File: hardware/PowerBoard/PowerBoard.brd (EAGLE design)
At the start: 90 x 56 mm, 136 parts, among them J1 CON-HRS-DM3AT, J2 CON-ZX62R-B-5P, J3 CON-FTSH-105-01-L-DV-K, J4 CON-S2B-PH-SM4-TB, J5 CON-PJ-102A, J6 CON-71741-0002-TOP, J7 SWITCH-CJS-1200-1200, M1 MOUNT-HOLE3.3, M2 MOUNT-HOLE3.3, M3 MOUNT-HOLE3.3, M4 MOUNT-HOLE3.3, M5 FIDUCIAL1X2, M6 FIDUCIAL1X2, M7 FIDUCIAL1X2, M8 FIDUCIAL1X2, Q1 SI2323CDS, Q2 SI2312CDS, Q3 SI2333CDS, Q4 SI2333CDS, SW1 SWITCH-SPST, SW2 SWITCH-MS12ASG30, SW3 SWITCH-ESWITCH-TL3340G, U1 LTC4361-2DC, U10 MAX9938FEUK, U11 MAX9938FEUK, U12 MAX9938FEUK, U13 STM32F10XCXT6, U14 LTC2942-1, U15 USBLC6-2, U2 LTC4085, U3 XC6220B331MR-G, U4 XC6220B331MR-G, U5 XC9236A15DMR-G, U6 MIC94043, U8 MAX9938FEUK, U9 MAX9938FEUK, X1 ECX-2236, X2 ECX-31B

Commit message: - Layout update
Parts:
- moved R12 0.50 mm to (36.0, 36.5)
- moved R14 0.50 mm to (41.6, 36.5)
- moved R41 0.50 mm to (38.8, 37.3)
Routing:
- net D1V5-EN: track 10.7 -> 11.2 mm
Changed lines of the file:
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@@
 <layer number="21" name="tPlace" color="7" fill="1" visible="no" active="yes"/>
 <layer number="22" name="bPlace" color="7" fill="1" visible="no" active="yes"/>
-<layer number="23" name="tOrigins" color="15" fill="1" visible="no" active="yes"/>
-<layer number="24" name="bOrigins" color="15" fill="1" visible="no" active="yes"/>
+<layer number="23" name="tOrigins" color="15" fill="1" visible="yes" active="yes"/>
+<layer number="24" name="bOrigins" color="15" fill="1" visible="yes" active="yes"/>
 <layer number="25" name="tNames" color="7" fill="1" visible="no" active="yes"/>
 <layer number="26" name="bNames" color="7" fill="1" visible="no" active="yes"/>
@@
 <element name="C9" library="powerboard" package="C0603" value="10uF" x="41.1" y="35.3" rot="R90"/>
 <element name="C10" library="powerboard" package="C0603" value="4.7uF" x="35" y="35.3" rot="R90"/>
-<element name="R41" library="powerboard" package="R0603" value="100k" x="39.3" y="37.3" rot="MR270">
-<attribute name="TOLERANCE" value="" x="39.3" y="37.3" size="1.778" layer="28" rot="MR270" display="off"/>
+<element name="R41" library="powerboard" package="R0603" value="100k" x="38.8" y="37.3" rot="MR270">
+<attribute name="TOLERANCE" value="" x="38.8" y="37.3" size="1.778" layer="28" rot="MR270" display="off"/>
 </element>
 <element name="C11" library="powerboard" package="C0603" value="4.7uF" x="45.2" y="35.8" rot="R90"/>
 <element name="C12" library="powerboard" package="C0603" value="10uF" x="50.2" y="35.8" rot="R270"/>
-<element name="R12" library="powerboard" package="R0603" value="0" x="36.5" y="36.5" rot="MR180">
-<attribute name="TOLERANCE" value="" x="36.5" y="36.5" size="1.778" layer="28" rot="MR180" display="off"/>
+<element name="R12" library="powerboard" package="R0603" value="0" x="36" y="36.5" rot="MR180">
+<attribute name="TOLERANCE" value="" x="36" y="36.5" size="1.778" layer="28" rot="MR180" display="off"/>
 </element>
 <element name="U14" library="powerboard" package="DFN-6" value="LTC2942-1" x="71.3" y="24.5" rot="R270">
@@
 <attribute name="MPN" value="FTSH-105-01-L-DV-K" x="6" y="31" size="1.778" layer="27" rot="R180" display="off"/>
 </element>
-<element name="R14" library="powerboard" package="R0603" value="0" x="42.1" y="36.5" rot="MR180">
-<attribute name="TOLERANCE" value="" x="42.1" y="36.5" size="1.778" layer="28" rot="MR180" display="off"/>
+<element name="R14" library="powerboard" package="R0603" value="0" x="41.6" y="36.5" rot="MR180">
+<attribute name="TOLERANCE" value="" x="41.6" y="36.5" size="1.778" layer="28" rot="MR180" display="off"/>
 </element>
 <element name="R13" library="powerboard" package="R0603" value="DNP" x="43.8" y="32.7" rot="MR180">
@@
 <wire x1="41" y1="31.9" x2="41" y2="34.1" width="0.8128" layer="1"/>
 <wire x1="48.1" y1="28.5" x2="47.7" y2="28.9" width="0.8128" layer="1"/>
-<wire x1="47.7" y1="28.9" x2="47.7" y2="31.1" width="0.8128" layer="1"/>
-<wire x1="47.7" y1="31.1" x2="46.9" y2="31.9" width="0.8128" layer="1"/>
-<wire x1="46.6" y1="31.9" x2="41" y2="31.9" width="0.8128" layer="1"/>
-<wire x1="46.6" y1="34.7" x2="46.6" y2="31.9" width="0.8128" layer="1"/>
+<wire x1="47.7" y1="28.9" x2="47.7" y2="31" width="0.8128" layer="1"/>
+<wire x1="47.7" y1="31" x2="46.8" y2="31.9" width="0.8128" layer="1"/>
+<wire x1="46.8" y1="31.9" x2="45.8" y2="31.9" width="0.8128" layer="1"/>
+<wire x1="45.7" y1="31.9" x2="41" y2="31.9" width="0.8128" layer="1"/>
+<wire x1="45.7" y1="34.7" x2="45.7" y2="31.9" width="0.8128" layer="1"/>
 <wire x1="43.5" y1="32.2" x2="43.2" y2="32.5" width="0.254" layer="1"/>
 <wire x1="43.2" y1="32.5" x2="43.1" y2="32.5" width="0.254" layer="1"/>
@@
 <wire x1="47.4" y1="37.8" x2="47.7" y2="37.95" width="0" layer="19" extent="16-16"/>
 <wire x1="46.75" y1="34.6" x2="46.8" y2="34.9" width="0" layer="19" extent="1-1"/>
-<wire x1="46.6" y1="34.7" x2="46.75" y2="34.6" width="0" layer="19" extent="1-1"/>
-<wire x1="46.45" y1="34.9" x2="46.6" y2="34.7" width="0" layer="19" extent="1-1"/>
+<wire x1="46.45" y1="34.9" x2="46.8" y2="34.9" width="0" layer="19" extent="1-1"/>
 <wire x1="45.2" y1="34.95" x2="45.4" y2="34.9" width="0" layer="19" extent="1-1"/>
-<wire x1="46.9" y1="31.9" x2="46.6" y2="31.9" width="0" layer="19" extent="1-1"/>
+<wire x1="45.7" y1="34.7" x2="45.4" y2="34.9" width="0" layer="19" extent="1-1"/>
+<wire x1="45.8" y1="31.9" x2="45.7" y2="31.9" width="0" layer="19" extent="1-1"/>
 <wire x1="40.9" y1="34.4" x2="41" y2="34.1" width="0" layer="19" extent="1-1"/>
 <wire x1="41.1" y1="34.45" x2="40.9" y2="34.4" width="0" layer="19" extent="1-1"/>
@@
 <via x="27.6" y="39.4" extent="1-16" drill="0.254"/>
 <via x="35" y="33.3" extent="1-16" drill="0.6"/>
-<wire x1="35.3" y1="34.4" x2="35" y2="34.1" width="0.8128" layer="1"/>
 <wire x1="35" y1="34.1" x2="35" y2="33.3" width="0.8128" layer="1"/>
 <via x="51.5" y="31.6" extent="1-16" drill="0.254"/>
@@
 <wire x1="41.3" y1="41.2" x2="40.95" y2="40.8" width="0" layer="19" extent="16-16"/>
 <wire x1="22.45" y1="24.3" x2="22.4" y2="24.3" width="0" layer="19" extent="16-16"/>
-<wire x1="36.8" y1="34.35" x2="36.7" y2="34.4" width="0" layer="19" extent="1-1"/>
 <wire x1="24.3" y1="16.75" x2="24.4" y2="16.8" width="0" layer="19" extent="16-16"/>
 <wire x1="22.3" y1="16.75" x2="22.4" y2="16.6" width="0" layer="19" extent="16-16"/>
@@
 <wire x1="23.35" y1="33.8" x2="23.5" y2="34" width="0" layer="19" extent="16-16"/>
 <wire x1="16.85" y1="26.4" x2="16.6" y2="26.4" width="0" layer="19" extent="1-1"/>
-<wire x1="35" y1="34.45" x2="35.3" y2="34.4" width="0" layer="19" extent="1-1"/>
 <wire x1="22.45" y1="26.3" x2="22.4" y2="26" width="0" layer="19" extent="16-16"/>
+<wire x1="35" y1="34.45" x2="35" y2="34.1" width="0" layer="19" extent="1-1"/>
+<wire x1="35.3" y1="34.4" x2="35" y2="34.45" width="0" layer="19" extent="1-1"/>
+<wire x1="36.8" y1="34.35" x2="36.7" y2="34.4" width="0" layer="19" extent="1-1"/>
 <wire x1="50.65" y1="28.5" x2="50.9" y2="28.2" width="0" layer="19" extent="16-16"/>
 <wire x1="44.05" y1="28.3" x2="43.7" y2="28.5" width="0" layer="19" extent="16-16"/>
@@
 <wire x1="25.1" y1="36.1" x2="25.1" y2="37" width="0.2032" layer="1"/>
 <wire x1="25.1" y1="37" x2="24.4" y2="37.7" width="0.2032" layer="1"/>
-<wire x1="35.3" y1="36.1" x2="35.65" y2="36.5" width="0" layer="19" extent="16-16"/>
+<wire x1="35.3" y1="36.1" x2="35.15" y2="36.5" width="0" layer="19" extent="16-16"/>
 <wire x1="24" y1="38.6" x2="24.4" y2="37.7" width="0" layer="19" extent="1-1"/>
 </signal>
@@
 <contactref element="R41" pad="2"/>
 <contactref element="R14" pad="1"/>
-<wire x1="41.3" y1="36.1" x2="38.2" y2="36.1" width="0.254" layer="16"/>
-<wire x1="38.2" y1="36.1" x2="37.6" y2="36.1" width="0.254" layer="16"/>
+<wire x1="40.8" y1="36.1" x2="37.7" y2="36.1" width="0.254" layer="16"/>
+<wire x1="37.7" y1="36.1" x2="37.1" y2="36.1" width="0.254" layer="16"/>
 <wire x1="48.6" y1="30.45" x2="48.6" y2="31.4" width="0.254" layer="1"/>
-<wire x1="48.6" y1="31.4" x2="47.5" y2="32.5" width="0.254" layer="1"/>
-<wire x1="47.5" y1="32.5" x2="47.5" y2="33.7" width="0.254" layer="1"/>
-<wire x1="47.5" y1="33.7" x2="38.2" y2="33.7" width="0.254" layer="16"/>
-<via x="47.5" y="33.7" extent="1-16" drill="0.254"/>
+<wire x1="48.6" y1="31.4" x2="46.9" y2="33.1" width="0.254" layer="1"/>
+<wire x1="46.9" y1="33.1" x2="46.9" y2="33.7" width="0.254" layer="1"/>
+<wire x1="46.9" y1="33.7" x2="37.7" y2="33.7" width="0.254" layer="16"/>
+<via x="46.9" y="33.7" extent="1-16" drill="0.254"/>
 <wire x1="43.9" y1="33.4" x2="44.2" y2="33.7" width="0.254" layer="1"/>
 <via x="44.2" y="33.7" extent="1-16" drill="0.254"/>
-<via x="38.2" y="33.7" extent="1-16" drill="0.254"/>
-<via x="38.2" y="36.1" extent="1-16" drill="0.254"/>
-<wire x1="38.2" y1="33.7" x2="38.2" y2="36.1" width="0.254" layer="1"/>
+<via x="37.7" y="33.7" extent="1-16" drill="0.254"/>
+<via x="37.7" y="36.1" extent="1-16" drill="0.254"/>
+<wire x1="37.7" y1="33.7" x2="37.7" y2="36.1" width="0.254" layer="1"/>
 <wire x1="48.6" y1="30.45" x2="48.9" y2="30.35" width="0" layer="19" extent="1-1"/>
-<wire x1="41.25" y1="36.5" x2="41.3" y2="36.1" width="0" layer="19" extent="16-16"/>
-<wire x1="37.35" y1="36.5" x2="37.6" y2="36.1" width="0" layer="19" extent="16-16"/>
-<wire x1="39.3" y1="36.45" x2="38.2" y2="36.1" width="0" layer="19" extent="16-16"/>
-<wire x1="44.2" y1="33.7" x2="47.5" y2="33.7" width="0" layer="19" extent="1-1"/>
+<wire x1="40.75" y1="36.5" x2="40.8" y2="36.1" width="0" layer="19" extent="16-16"/>
+<wire x1="36.85" y1="36.5" x2="37.1" y2="36.1" width="0" layer="19" extent="16-16"/>
+<wire x1="38.8" y1="36.45" x2="37.7" y2="36.1" width="0" layer="19" extent="16-16"/>
+<wire x1="44.2" y1="33.7" x2="46.9" y2="33.7" width="0" layer="19" extent="1-1"/>
 <wire x1="43.793465625" y1="33.1" x2="43.9" y2="33.4" width="0" layer="19" extent="1-1"/>
 </signal>
@@
 <wire x1="47.9" y1="33.1" x2="48.5" y2="33.7" width="0.254" layer="16"/>
 <via x="48.5" y="36.1" extent="1-16" drill="0.254"/>
-<wire x1="43.3" y1="36.1" x2="48.5" y2="36.1" width="0.254" layer="16"/>
+<wire x1="42.8" y1="36.1" x2="48.5" y2="36.1" width="0.254" layer="16"/>
 <wire x1="48.5" y1="36.1" x2="48.5" y2="35.1" width="0.254" layer="1"/>
 <via x="48.5" y="33.7" extent="1-16" drill="0.254"/>
@@
 <wire x1="44.65" y1="32.7" x2="44.7" y2="33.1" width="0" layer="19" extent="16-16"/>
 <wire x1="48.5" y1="35.1" x2="48.65" y2="34.6" width="0" layer="19" extent="1-1"/>
-<wire x1="42.95" y1="36.5" x2="43.3" y2="36.1" width="0" layer="19" extent="16-16"/>
-<wire x1="44.9" y1="36.55" x2="43.3" y2="36.1" width="0" layer="19" extent="16-16"/>
+<wire x1="42.45" y1="36.5" x2="42.8" y2="36.1" width="0" layer="19" extent="16-16"/>
+<wire x1="44.9" y1="36.55" x2="42.8" y2="36.1" width="0" layer="19" extent="16-16"/>
 </signal>
 <signal name="N$5">

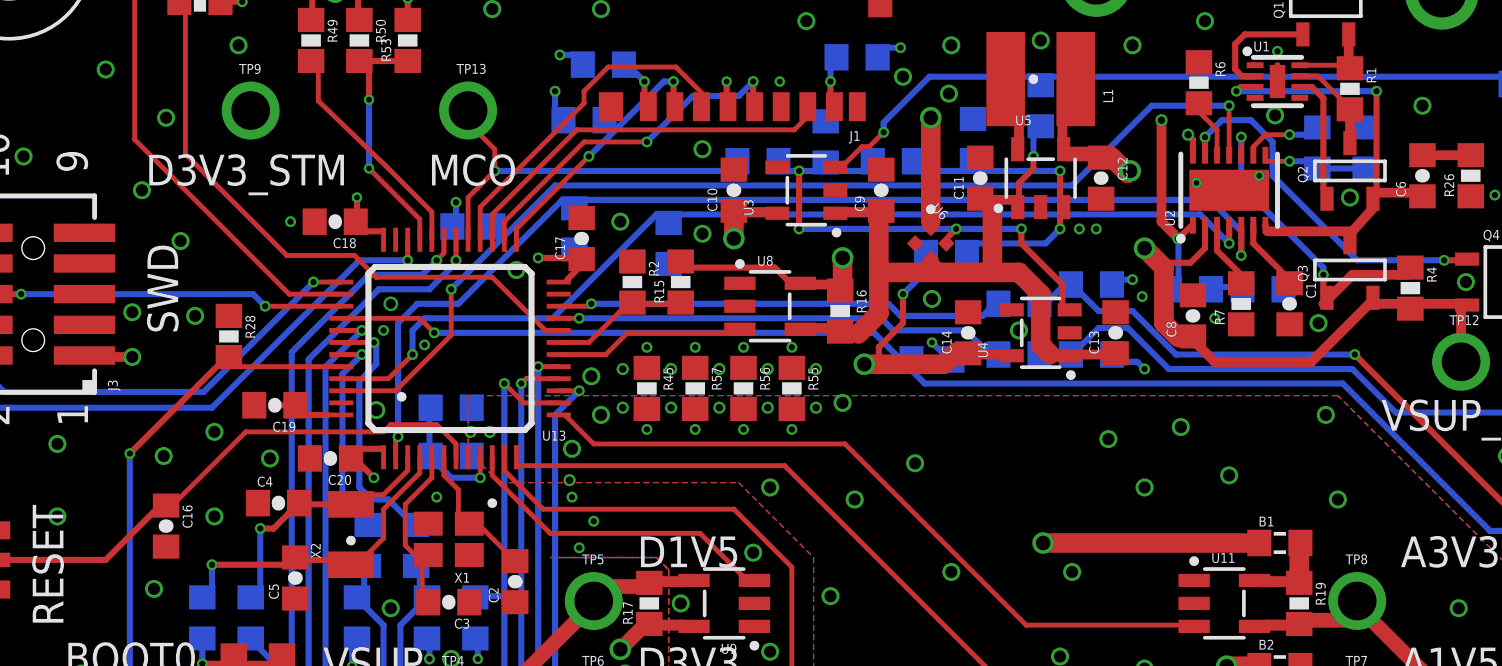
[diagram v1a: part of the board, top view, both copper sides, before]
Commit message: - Decoupling capacitors moved to ICs on schematic - Layout update
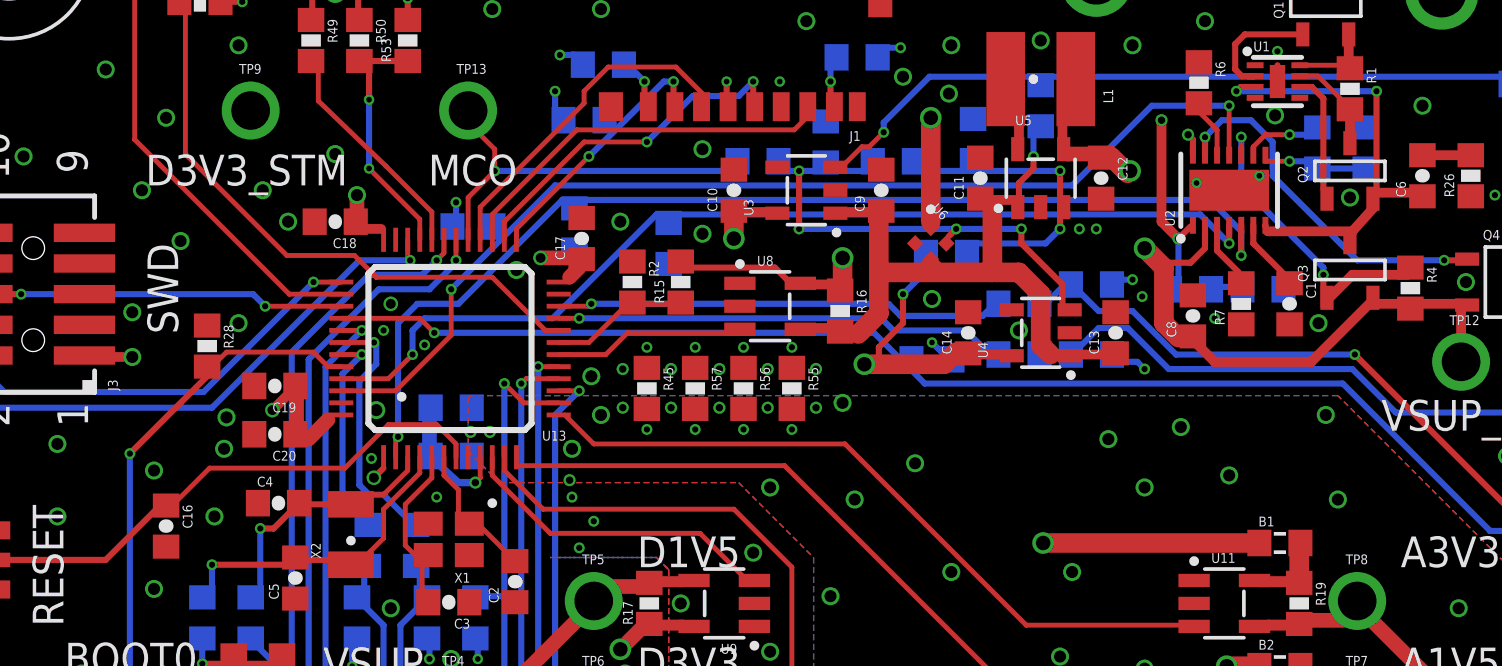
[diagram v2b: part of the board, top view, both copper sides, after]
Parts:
- moved C20 2.51 mm to (16.0, 25.2)
- moved R28 0.98 mm to (13.2, 28.9)
- moved C19 0.80 mm to (16.0, 27.2)
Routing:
- net DGND: vias 153 -> 156

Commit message: - Air wires eliminated
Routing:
- net D3V3_STM: track 29.9 -> 41.8 mm
- net VSUP_I: track 26.2 -> 33.3 mm
- net VSUP_R: track 39.8 -> 45.0 mm
- net D3V3_I: track 21.0 -> 24.3 mm
- net D3V3: track 15.9 -> 18.8 mm
- net D3V3_STM-EN-SW: track 15.9 -> 18.5 mm
- net D1V5_I: track 9.61 -> 12.2 mm
- net D1V5-EN: track 11.2 -> 13.7 mm
- net D1V5: track 11.8 -> 14.0 mm
- net PC15-S: track 10.5 -> 12.6 mm
- net PA8-EN: track 19.7 -> 21.5 mm
- net VBAT_I: track 7.03 -> 8.77 mm
- net WALL_P: track 17.4 -> 19.0 mm
- net PA8: track 15.4 -> 16.9 mm
- net PC14-S: track 9.30 -> 10.8 mm
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
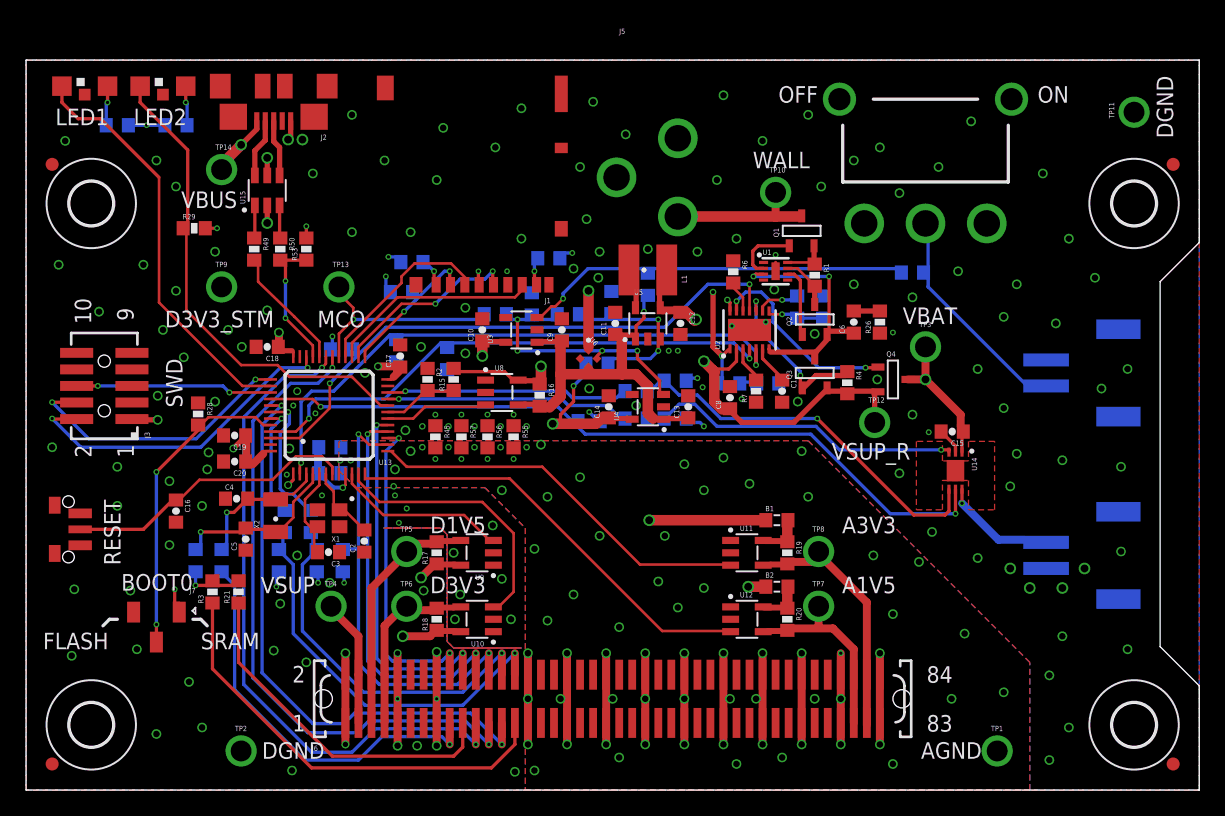
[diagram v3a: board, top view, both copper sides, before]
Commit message: - No airwires - AGND covers current sense - AGND, DGND measurement points moved
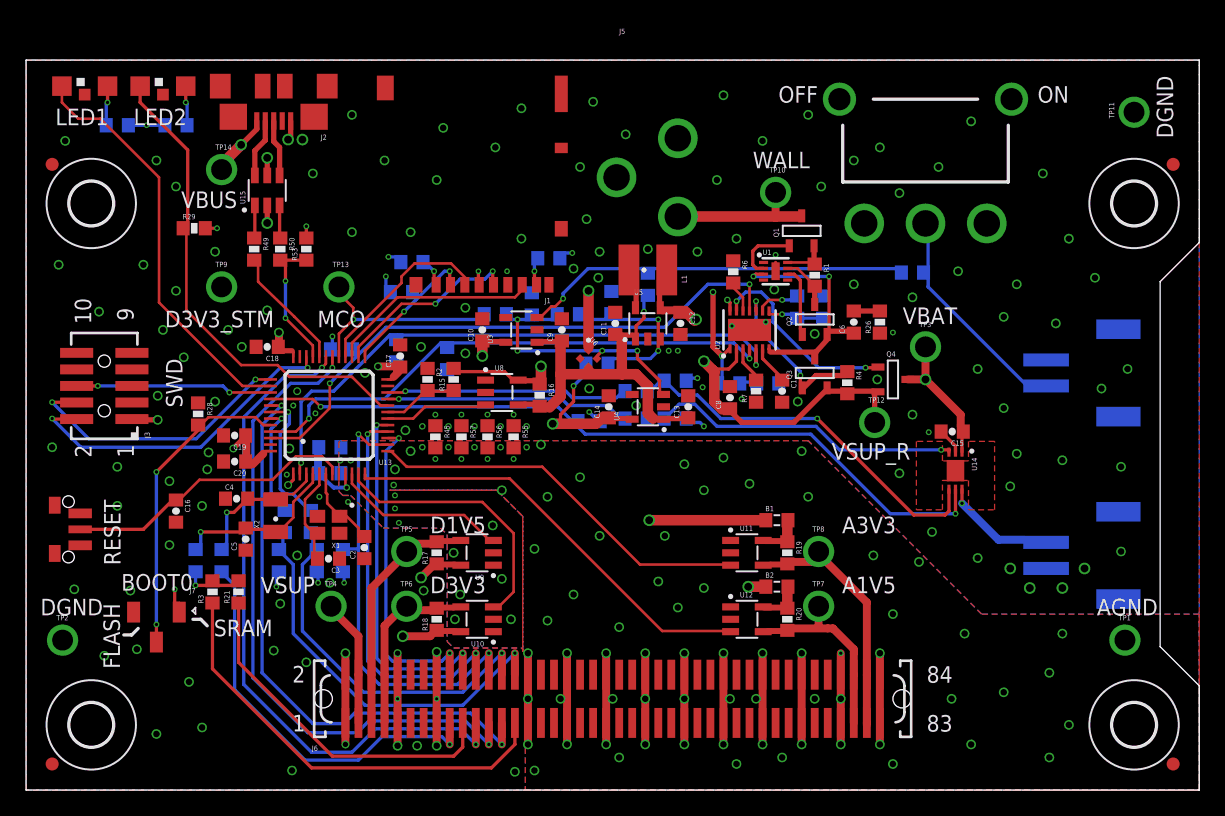
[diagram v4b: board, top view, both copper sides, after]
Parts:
- moved LOGO6 77.0 mm to (70.0, 2.50)
- moved LOGO5 66.5 mm to (11.0, 1.50)
- moved LOGO1 50.4 mm to (74.5, 15.2)
- moved LOGO7 44.5 mm to (74.5, 28.0)
- moved TP2 16.1 mm to (2.80, 11.5)
- moved TP1 13.0 mm to (84.3, 11.5)
- moved C2 0.50 mm to (25.9, 18.6)
- moved C3 0.50 mm to (23.2, 17.8)
- moved X1 0.50 mm to (23.2, 20.4)
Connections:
- net AGND: now also U10.1, U10.2, U9.1, U9.2
- net DGND: no longer U10.1, U10.2, U9.1, U9.2
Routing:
- net A3V3: track 16.7 -> 20.4 mm
- net A1V5: track 12.8 -> 15.9 mm
- net D3V3_STM: track 41.8 -> 43.5 mm
- net VSUP: track 13.4 -> 14.6 mm
- net BOOT0: track 23.2 -> 24.4 mm
- net OSC_OUT: track 5.99 -> 7.06 mm
- net PC15-S: track 12.6 -> 13.6 mm
- net A1V5_SENSE: track 32.2 -> 33.3 mm
- net PB2: track 37.0 -> 38.0 mm
- net VSUP_I: track 33.3 -> 34.2 mm
- net A1V5_I: track 3.00 -> 3.90 mm
- net OSC_IN: track 7.47 -> 8.32 mm
- net A3V3_I: track 3.20 -> 4.00 mm
- net NRST: track 22.1 -> 22.9 mm
- net WALL: track 10.6 -> 11.4 mm
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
